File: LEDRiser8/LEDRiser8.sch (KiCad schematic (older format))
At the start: 17 parts, among them J1 Conn_01x09_Male

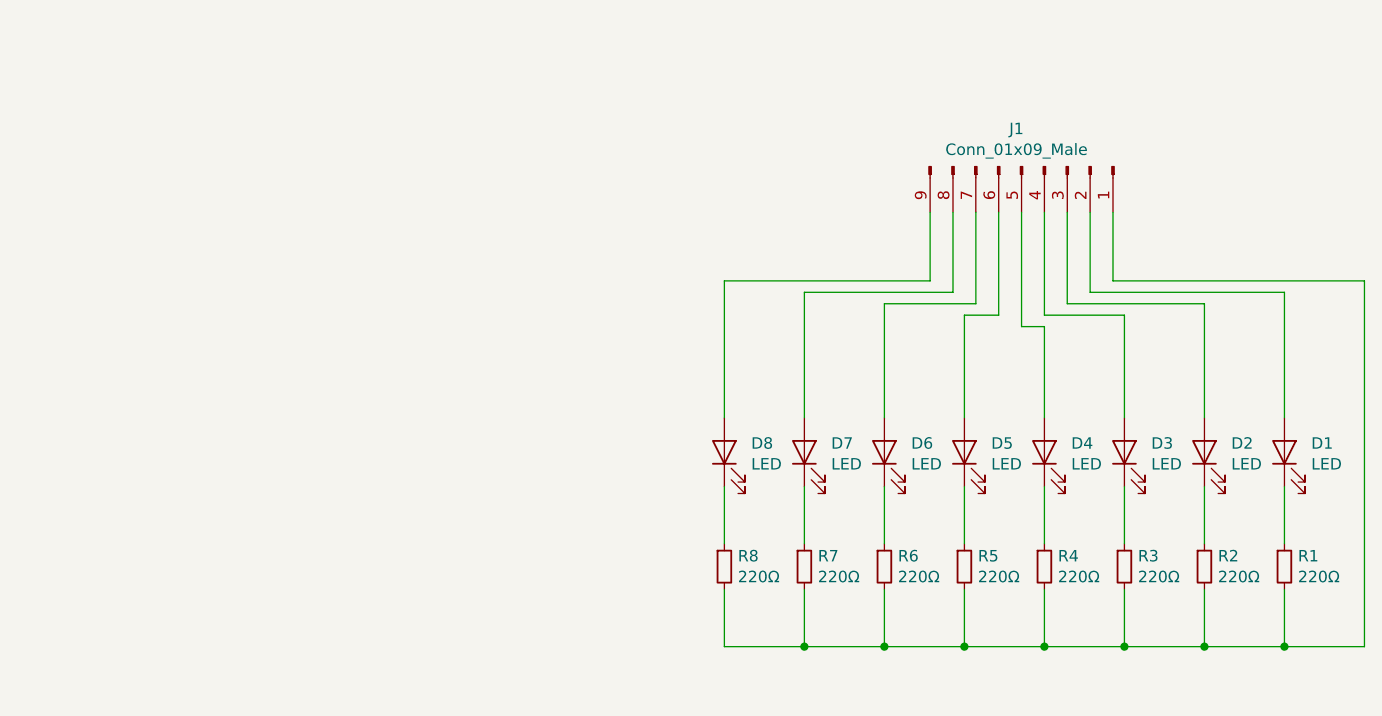
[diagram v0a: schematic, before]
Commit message: Update eight bit LED riser board to better match the sixteen bit version.
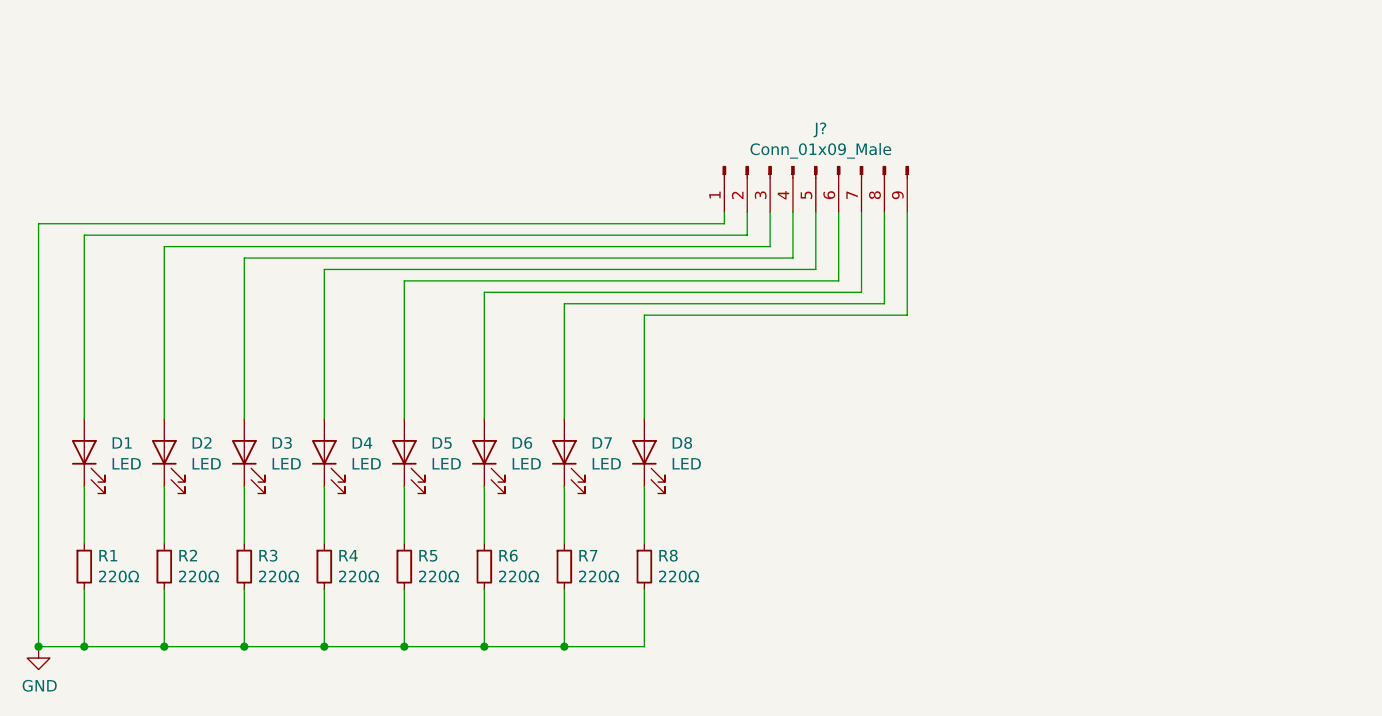
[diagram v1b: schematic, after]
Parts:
- removed J1: Conn_01x09_Male, Connector_PinHeader_2.54mm:PinHeader_1x09_P2.54mm_Vertical, symbol Connector:Conn_01x09_Male
- added J?: Conn_01x09_Male, symbol Connector:Conn_01x09_Male
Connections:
- net GND: now reaches R1.2, R2.2, R3.2, R4.2, R5.2, R6.2, R7.2, R8.2
- net GND: now also J?.1 (Pin_1)
- net at D1.2 (A): now also J?.2 (Pin_2)
- net at D2.2 (A): now also J?.3 (Pin_3)
- net at D3.2 (A): now also J?.4 (Pin_4)
- net at D4.2 (A): now also J?.5 (Pin_5)
- net at D5.2 (A): now also J?.6 (Pin_6)
- net at D6.2 (A): now also J?.7 (Pin_7)
- net at D7.2 (A): now also J?.8 (Pin_8)
- net at D8.2 (A): now also J?.9 (Pin_9)

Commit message: Added my name to the PCB silkscreen
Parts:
- J1: renamed from J?; footprint (none) -> Connector_PinHeader_2.54mm:PinHeader_1x09_P2.54mm_Vertical
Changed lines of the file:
@@
 Connection ~ 1450 4850
 $Comp
-L Connector:Conn_01x09_Male J?
+L Connector:Conn_01x09_Male J1
 U 1 1 5D8F9D32
 P 4650 2750
-F 0 "J?" V 4485 2728 50  0000 C CNN
+F 0 "J1" V 4485 2728 50  0000 C CNN
 F 1 "Conn_01x09_Male" V 4576 2728 50  0000 C CNN
-F 2 "" H 4650 2750 50  0001 C CNN
+F 2 "Connector_PinHeader_2.54mm:PinHeader_1x09_P2.54mm_Vertical" H 4650 2750 50  0001 C CNN
 F 3 "~" H 4650 2750 50  0001 C CNN
 	1    4650 2750

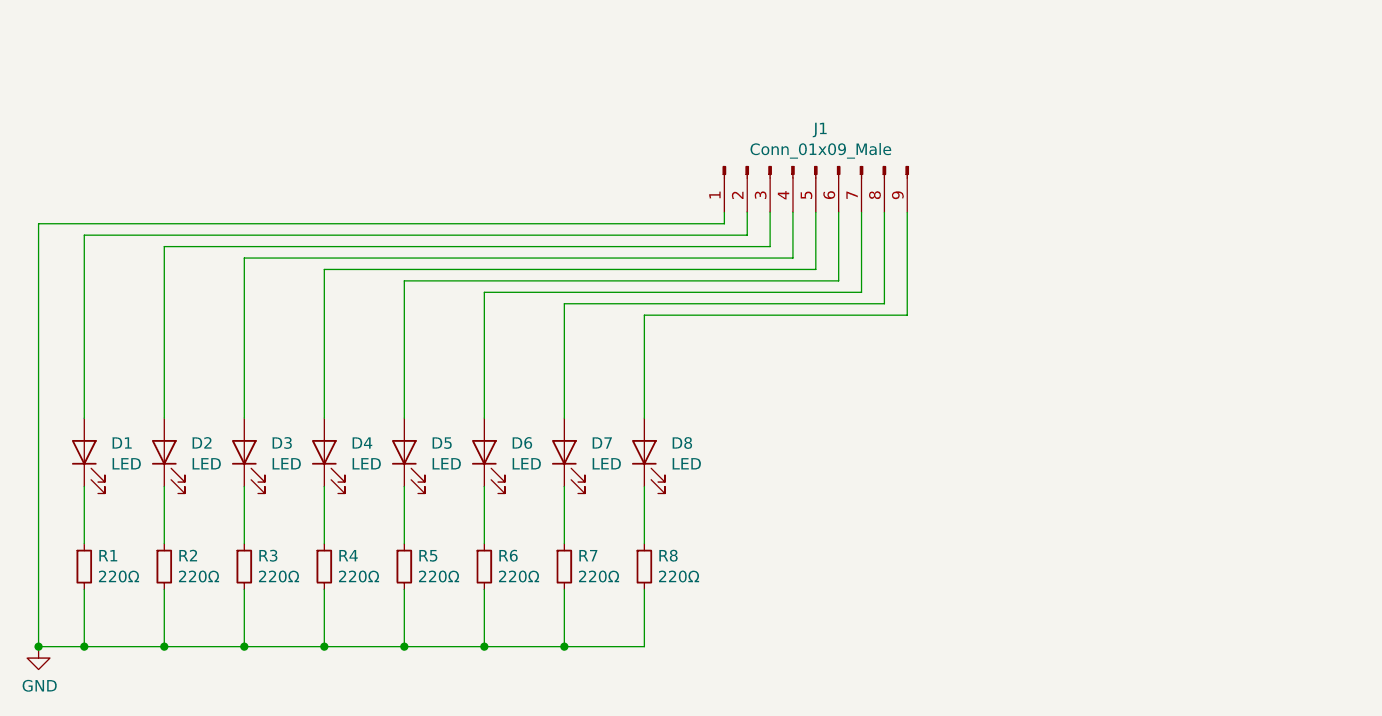
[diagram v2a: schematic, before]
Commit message: Use THT LED arrays for the 8-bit riser boards too.
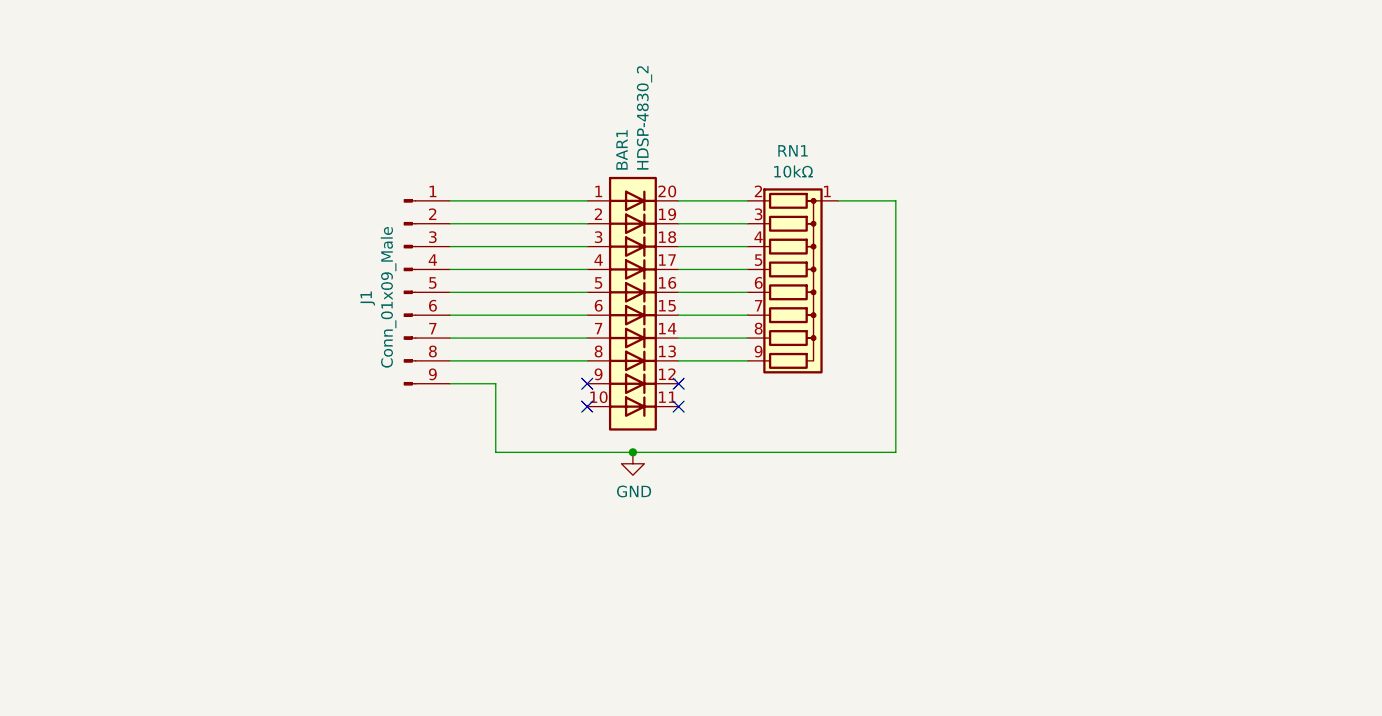
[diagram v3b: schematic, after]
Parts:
- removed D1, D2, D3, D4, D5, D6, D7, D8: LED, LED_SMD:LED_0603_1608Metric, symbol Device:LED
- removed R1, R2, R3, R4, R5, R6, R7, R8: 220Ω, Resistor_SMD:R_0603_1608Metric, symbol Device:R_Small
- added BAR1: HDSP-4830_2, Display:HDSP-4830, symbol LED:HDSP-4830_2
- added RN1: 10kΩ, Resistor_THT:R_Array_SIP9, symbol Device:R_Network08
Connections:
- net GND: now also J1.9 (Pin_9), RN1.1 (common); no longer J1.1 (Pin_1)
- net at J1.8 (Pin_8): now also BAR1.8 (A)
- net at J1.6 (Pin_6): now also BAR1.6 (A)
- net at J1.5 (Pin_5): now also BAR1.5 (A)
- net at J1.4 (Pin_4): now also BAR1.4 (A)
- net at J1.3 (Pin_3): now also BAR1.3 (A)
- net at J1.2 (Pin_2): now also BAR1.2 (A)
- net at J1.7 (Pin_7): now also BAR1.7 (A)
- new net: BAR1.1 (A), J1.1 (Pin_1)
- new net: BAR1.13 (K), RN1.9 (R8)
- new net: BAR1.14 (K), RN1.8 (R7)
- new net: BAR1.15 (K), RN1.7 (R6)
- new net: BAR1.16 (K), RN1.6 (R5)
- new net: BAR1.17 (K), RN1.5 (R4)
- new net: BAR1.18 (K), RN1.4 (R3)
- new net: BAR1.19 (K), RN1.3 (R2)
- new net: BAR1.20 (K), RN1.2 (R1)
- no-connect marks 0 -> 4

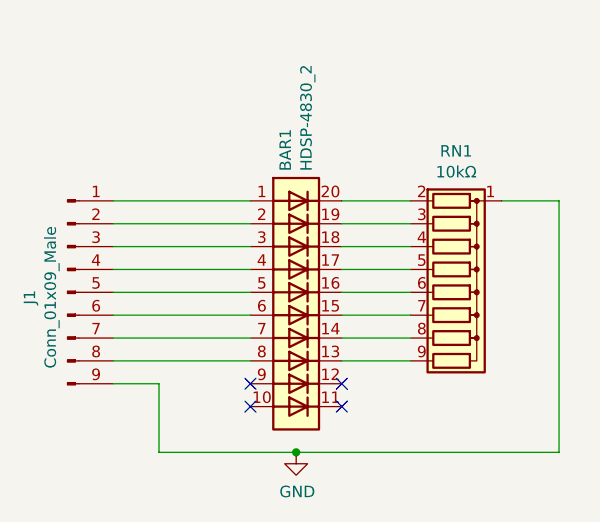
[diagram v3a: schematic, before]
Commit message: Route a 8-bit THT PCB for LED riser boards.
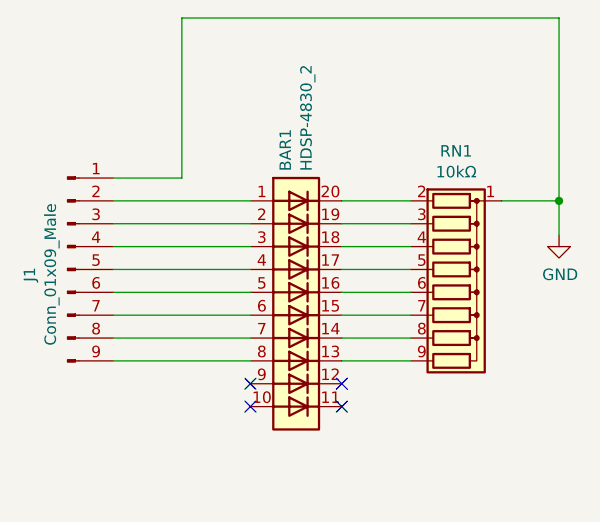
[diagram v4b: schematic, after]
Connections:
- net GND: now also J1.1 (Pin_1); no longer J1.9 (Pin_9)
- net at BAR1.1 (A): now also J1.2 (Pin_2); no longer J1.1 (Pin_1)
- net at BAR1.2 (A): now also J1.3 (Pin_3); no longer J1.2 (Pin_2)
- net at BAR1.3 (A): now also J1.4 (Pin_4); no longer J1.3 (Pin_3)
- net at BAR1.4 (A): now also J1.5 (Pin_5); no longer J1.4 (Pin_4)
- net at BAR1.5 (A): now also J1.6 (Pin_6); no longer J1.5 (Pin_5)
- net at BAR1.6 (A): now also J1.7 (Pin_7); no longer J1.6 (Pin_6)
- net at BAR1.7 (A): now also J1.8 (Pin_8); no longer J1.7 (Pin_7)
- net at BAR1.8 (A): now also J1.9 (Pin_9); no longer J1.8 (Pin_8)
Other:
- moved on the sheet: J1
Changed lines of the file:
@@
 Comment4 "LED riser board with eight LEDs and a ground pin."
 $EndDescr
+$Comp
+L LED:HDSP-4830_2 BAR1
+U 1 1 5D84B6C6
+P 3850 3300
+F 0 "BAR1" V 3804 3830 50  0000 L CNN
+F 1 "HDSP-4830_2" V 3895 3830 50  0000 L CNN
+F 2 "Display:HDSP-4830" H 3850 2500 50  0001 C CNN
+F 3 "https://docs.broadcom.com/docs/AV02-1798EN" H 1850 3500 50  0001 C CNN
+	1    3850 3300
+	1    0    0    -1
+$EndComp
+$Comp
+L Connector:Conn_01x09_Male J1
+U 1 1 5D836F73
+P 2850 3200
+F 0 "J1" V 2685 3178 50  0000 C CNN
+F 1 "Conn_01x09_Male" V 2776 3178 50  0000 C CNN
+F 2 "Connector_PinHeader_2.54mm:PinHeader_1x09_P2.54mm_Vertical" H 2850 3200 50  0001 C CNN
+F 3 "~" H 2850 3200 50  0001 C CNN
+	1    2850 3200
+	1    0    0    -1
+$EndComp
 Wire Wire Line
 	3050 2900 3650 2900
@@
 L power:GND #PWR01
 U 1 1 5D873AB0
-P 3850 4000
-F 0 "#PWR01" H 3850 3750 50  0001 C CNN
-F 1 "GND" H 3855 3827 50  0000 C CNN
-F 2 "" H 3850 4000 50  0001 C CNN
-F 3 "" H 3850 4000 50  0001 C CNN
-	1    3850 4000
+P 5000 3050
+F 0 "#PWR01" H 5000 2800 50  0001 C CNN
+F 1 "GND" H 5005 2877 50  0000 C CNN
+F 2 "" H 5000 3050 50  0001 C CNN
+F 3 "" H 5000 3050 50  0001 C CNN
+	1    5000 3050
 	1    0    0    -1
 $EndComp
@@
 	4750 2900 5000 2900
 Wire Wire Line
-	5000 4000 3850 4000
+	3050 2800 3350 2800
 Wire Wire Line
-	5000 2900 5000 4000
-$Comp
-L LED:HDSP-4830_2 BAR1
-U 1 1 5D84B6C6
-P 3850 3300
-F 0 "BAR1" V 3804 3830 50  0000 L CNN
-F 1 "HDSP-4830_2" V 3895 3830 50  0000 L CNN
-F 2 "Display:HDSP-4830" H 3850 2500 50  0001 C CNN
-F 3 "https://docs.broadcom.com/docs/AV02-1798EN" H 1850 3500 50  0001 C CNN
-	1    3850 3300
-	1    0    0    -1
-$EndComp
-$Comp
-L Connector:Conn_01x09_Male J1
-U 1 1 5D836F73
-P 2850 3300
-F 0 "J1" V 2685 3278 50  0000 C CNN
-F 1 "Conn_01x09_Male" V 2776 3278 50  0000 C CNN
-F 2 "Connector_PinHeader_2.54mm:PinHeader_1x09_P2.54mm_Vertical" H 2850 3300 50  0001 C CNN
-F 3 "~" H 2850 3300 50  0001 C CNN
-	1    2850 3300
-	1    0    0    -1
-$EndComp
-NoConn ~ 3650 3800
+	3350 2800 3350 2100
+Wire Wire Line
+	3350 2100 5000 2100
+Wire Wire Line
+	5000 2100 5000 2900
+NoConn ~ 4050 3700
 NoConn ~ 4050 3800
 NoConn ~ 3650 3700
-NoConn ~ 4050 3700
+NoConn ~ 3650 3800
 Wire Wire Line
-	3050 3700 3250 3700
-Wire Wire Line
-	3250 3700 3250 4000
-Wire Wire Line
-	3250 4000 3850 4000
-Connection ~ 3850 4000
+	5000 2900 5000 3050
+Connection ~ 5000 2900
 $EndSCHEMATC
